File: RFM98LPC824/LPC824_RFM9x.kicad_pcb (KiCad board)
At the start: 2 copper layers, 38.9 x 16.5 mm, 18 parts, among them J2 Conn_01x03, J3 Conn_01x06, J4 Conn_01x06, U1 LPC824M201JDH20, U2 RFM92/95/96/97/98, U3 AT25_EEPROM

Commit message: add missing RFM_CS trace
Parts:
- removed TP7: TEST, Measurement_Points:Measurement_Point_Round-SMD-Pad_Small
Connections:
- U1 pad 20: GPIO14 -> RFM_CS
- U2 pad 5: CS_RFM -> RFM_CS
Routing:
- net RFM_CS: track 0.00 -> 13.5 mm, vias 0 -> 2
- net GPIO14: track 2.14 -> 0.00 mm, vias 1 -> 0
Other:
- board text added: "V2.0.1"
- board text added: "V2.0.1 2018-04-15"
- board text removed: "V2.0.0"
- board text removed: "V2.0.0 2018-04-14"

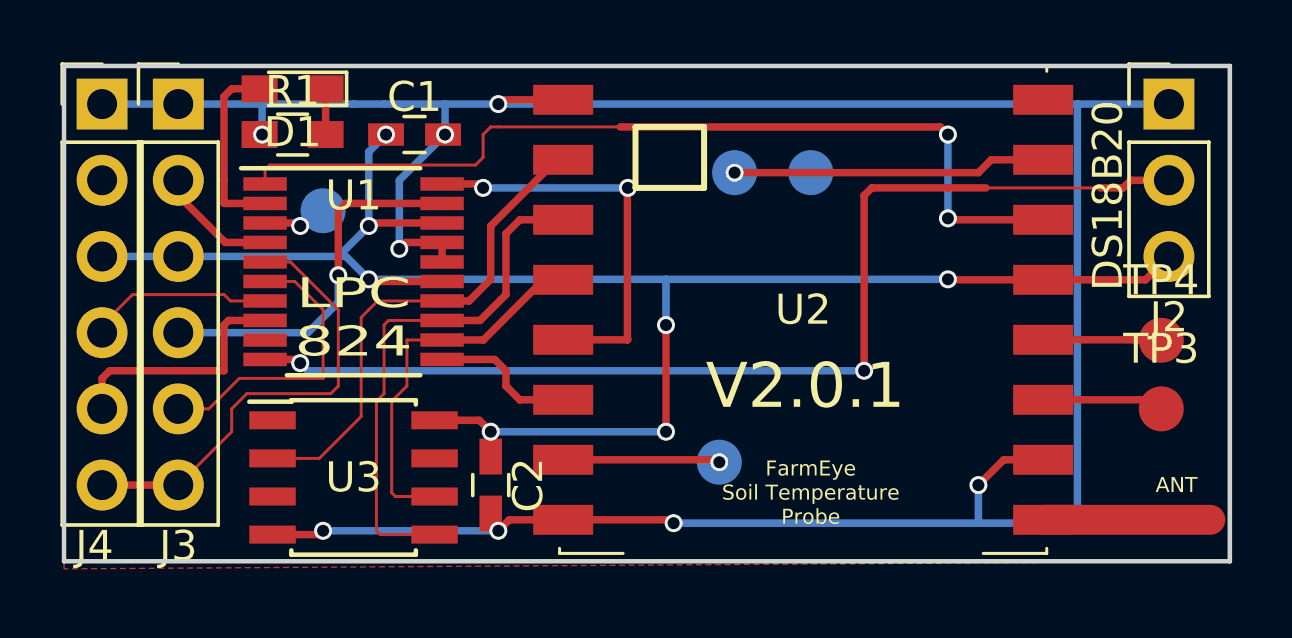
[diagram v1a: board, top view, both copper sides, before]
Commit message: add GPIO11 test pad
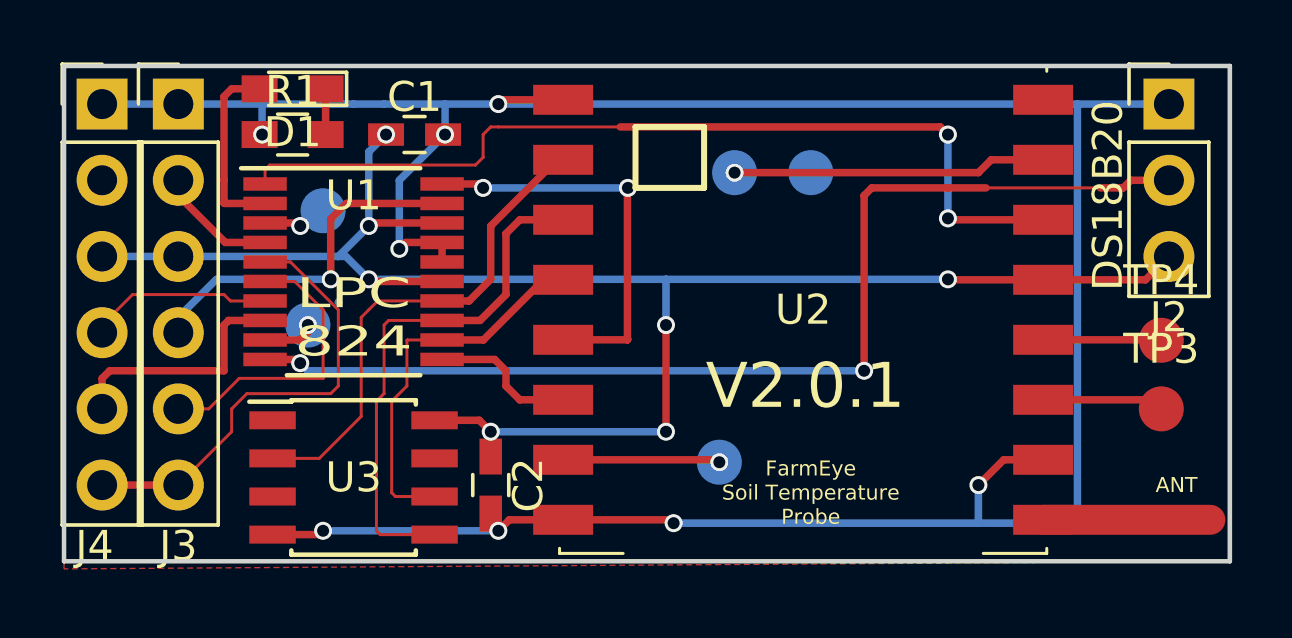
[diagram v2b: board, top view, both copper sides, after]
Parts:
- added TP8: TEST, Measurement_Points:Measurement_Point_Round-SMD-Pad_Small, B.Cu at (149.1, 106.4)
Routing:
- net GPIO11: track 0.00 -> 1.77 mm, vias 0 -> 1
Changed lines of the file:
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@@
 (kicad_pcb (version 4) (host pcbnew 4.0.7-e2-6376~58~ubuntu15.04.1)
   (general
-    (links 44)
+    (links 45)
     (no_connects 1)
     (area 140.894999 97.714999 179.907001 114.375001)
     (thickness 1.6)
     (drawings 32)
-    (tracks 219)
+    (tracks 223)
     (zones 0)
-    (modules 17)
+    (modules 18)
     (nets 30)
   )
@@
       (xy -0.117902 -2.924174) (xy -0.057389 -2.933563) (xy -0.006332 -2.910978)) (layer B.Mask) (width 0.01))
   )
+  (module Measurement_Points:Measurement_Point_Round-SMD-Pad_Small (layer B.Cu)
+    (at 149.098 106.426)
+    (descr "Mesurement Point, Round, SMD Pad, DM 1.5mm,")
+    (tags "Mesurement Point Round SMD Pad 1.5mm")
+    (attr virtual)
+    (fp_text reference TP8 (at 0 2) (layer B.SilkS)
+      (effects (font (size 1 1) (thickness 0.15)) (justify mirror))
+    )
+    (fp_text value TEST (at 0 -2) (layer B.Fab)
+      (effects (font (size 1 1) (thickness 0.15)) (justify mirror))
+    )
+    (fp_circle (center 0 0) (end 1 0) (layer B.CrtYd) (width 0.05))
+    (pad 1 smd circle (at 0 0) (size 1.5 1.5) (layers B.Cu B.Mask)
+      (net 28 GPIO11))
+  )
   (gr_text ANT (at 178.054 111.76) (layer F.SilkS)
     (effects (font (size 0.5 0.5) (thickness 0.1)))
@@
     (arrow2b (pts (xy 184.785 97.79) (xy 185.371421 98.916504)))
   )
+  (segment (start 150.111558 105.661558) (end 150.114 105.664) (width 0.25) (layer B.Cu) (net 0))
   (segment (start 157.608 98.918) (end 155.59 98.918) (width 0.25) (layer F.Cu) (net 1))
   (via (at 155.448 99.06) (size 0.6) (drill 0.4) (layers F.Cu B.Cu) (net 1))
@@
   (segment (start 155.702 108.458) (end 155.702 107.95) (width 0.25) (layer F.Cu) (net 15))
   (segment (start 156.162 108.918) (end 155.702 108.458) (width 0.25) (layer F.Cu) (net 15))
-  (segment (start 150.111558 104.767442) (end 150.111558 105.661558) (width 0.25) (layer B.Cu) (net 16))
-  (segment (start 150.111558 105.661558) (end 150.114 105.664) (width 0.25) (layer B.Cu) (net 16))
-  (segment (start 150.357 102.373) (end 150.111558 102.618442) (width 0.25) (layer F.Cu) (net 16))
-  (segment (start 150.111558 102.618442) (end 150.111558 104.767442) (width 0.25) (layer F.Cu) (net 16))
-  (via (at 150.111558 104.767442) (size 0.6) (drill 0.4) (layers F.Cu B.Cu) (net 16))
-  (segment (start 153.572 102.373) (end 150.357 102.373) (width 0.25) (layer F.Cu) (net 16))
-  (segment (start 149.098 106.68) (end 144.78 106.68) (width 0.25) (layer B.Cu) (net 16))
-  (segment (start 150.114 105.664) (end 149.098 106.68) (width 0.25) (layer B.Cu) (net 16))
+  (segment (start 153.572 102.373) (end 150.379 102.373) (width 0.25) (layer F.Cu) (net 16))
+  (segment (start 146.05 104.902) (end 144.78 106.172) (width 0.25) (layer B.Cu) (net 16))
+  (segment (start 149.86 104.902) (end 146.05 104.902) (width 0.25) (layer B.Cu) (net 16))
+  (via (at 149.86 104.902) (size 0.6) (drill 0.4) (layers F.Cu B.Cu) (net 16))
+  (segment (start 149.86 102.892) (end 149.86 104.902) (width 0.25) (layer F.Cu) (net 16))
+  (segment (start 150.379 102.373) (end 149.86 102.892) (width 0.25) (layer F.Cu) (net 16))
+  (segment (start 144.78 106.172) (end 144.78 106.68) (width 0.25) (layer B.Cu) (net 16))
   (segment (start 149.69 98.552) (end 149.69 100.076) (width 0.25) (layer F.Cu) (net 17))
   (segment (start 146.304 101.6) (end 146.304 102.362) (width 0.25) (layer F.Cu) (net 18))
@@
   (segment (start 173.608 98.918) (end 172.862 98.918) (width 0.25) (layer F.Cu) (net 27))
   (segment (start 173.608 98.918) (end 173.116 98.918) (width 0.25) (layer F.Cu) (net 27))
+  (segment (start 147.672 106.923) (end 148.833 106.923) (width 0.25) (layer F.Cu) (net 28))
+  (via (at 149.098 106.426) (size 0.6) (drill 0.4) (layers F.Cu B.Cu) (net 28))
+  (segment (start 149.098 106.658) (end 149.098 106.426) (width 0.25) (layer F.Cu) (net 28))
+  (segment (start 148.833 106.923) (end 149.098 106.658) (width 0.25) (layer F.Cu) (net 28))
   (segment (start 159.75 106.918) (end 159.75 101.87) (width 0.25) (layer F.Cu) (net 29))
-  (segment (start 154.809 101.723) (end 153.572 101.723) (width 0.25) (layer F.Cu) (net 29) (status 800000))
+  (segment (start 154.809 101.723) (end 153.572 101.723) (width 0.25) (layer F.Cu) (net 29))
   (segment (start 154.94 101.854) (end 154.809 101.723) (width 0.25) (layer F.Cu) (net 29))
   (via (at 154.94 101.854) (size 0.6) (drill 0.4) (layers F.Cu B.Cu) (net 29))

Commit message: LPC824/RFM9x board v2.0.1
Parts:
- removed TP6, TP8: TEST, Measurement_Points:Measurement_Point_Round-SMD-Pad_Small
- U1: footprint Housings_SSOP:TSSOP-20_4.4x6.5mm_Pitch0.65mm -> TSSOP20_handsolder:TSSOP-20_4.4x6.5mm_Pitch0.65mm
- U3: footprint Housings_SOIC:SOIC-8_3.9x4.9mm_Pitch1.27mm -> adafruit:SO08
- moved C2 0.51 mm to (155.7, 111.8)
- turned U3 to 270 degrees
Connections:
- J4 pad 2: Net-(J4-Pad2) -> GPIO13
- U1 pad 9: GPIO11 -> FLASH_CS
- U3 pad 1: CS_FLM -> FLASH_CS
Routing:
- net DIO2: track 1.24 -> 9.45 mm, vias 0 -> 1
- net FLASH_CS: track 0.00 -> 8.10 mm, vias 0 -> 2
- net GPIO13: track 2.19 -> 8.60 mm
- net GND: track 91.1 -> 93.6 mm
- net GPIO11: track 1.77 -> 0.00 mm, vias 1 -> 0
- net SWCLK: track 6.20 -> 7.50 mm
- net MISO: track 16.8 -> 17.6 mm
- net SWDIO: track 8.14 -> 7.55 mm
- net TXD: track 9.86 -> 10.4 mm
